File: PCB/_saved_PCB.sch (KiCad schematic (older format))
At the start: 9 parts, among them P1 Power, P2 Analog, P3 Digital, P4 Digital, P5 CONN_01X01, P6 CONN_01X01, P7 CONN_01X01, P8 CONN_01X01

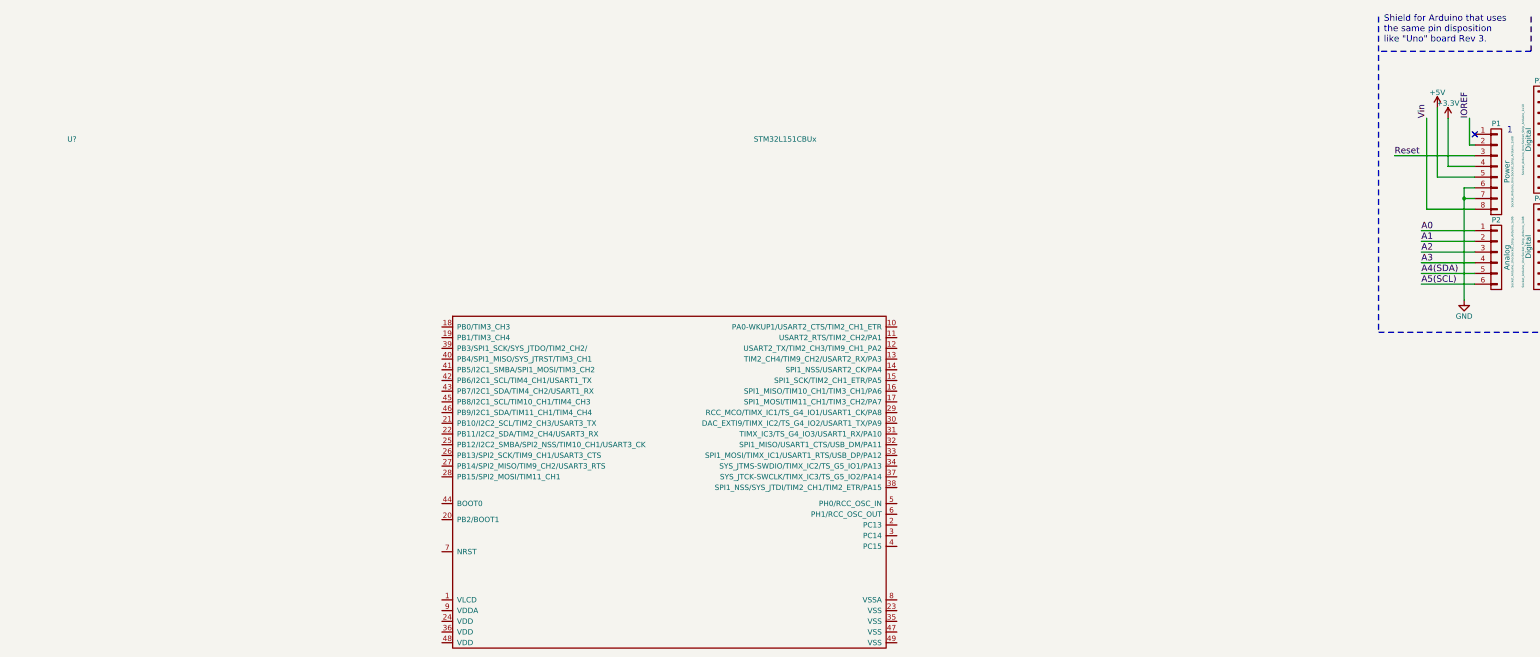
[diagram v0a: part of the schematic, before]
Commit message: add license
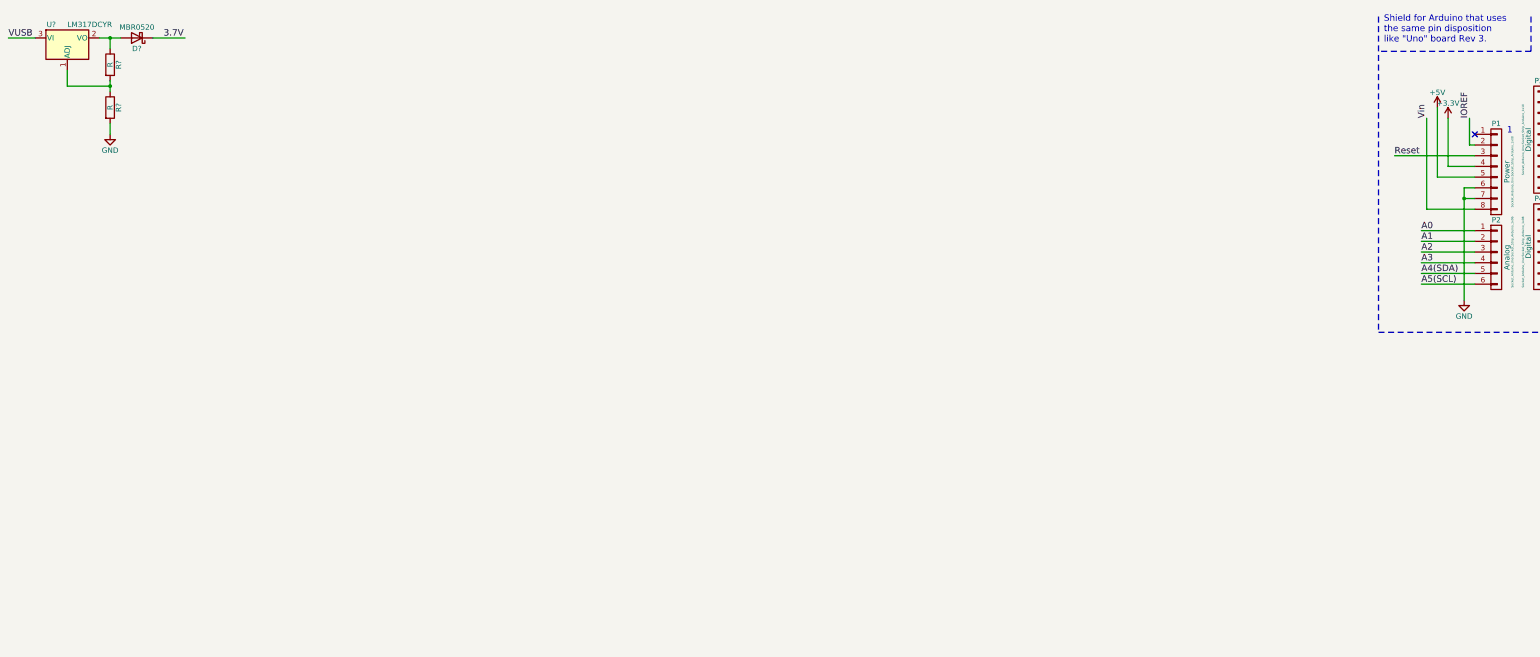
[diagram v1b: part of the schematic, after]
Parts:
- removed U?: STM32L151CBUx, UFQFPN48, symbol STM32L151CBUx
- added D?: MBR0520, Diode_SMD:D_SOD-123, symbol MBR0520
- added R? (x2): R, symbol R
- added U?: LM317DCYR, symbol LM317_3PinPackage
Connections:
- net GND: now also R?.2
- new net: R?.1, R?.2, U?.1 (ADJ)
- new net: D?.2 (A), R?.1, U?.2 (VO)
- new net 3.7V: D?.1 (K)
- new net VUSB: U?.3 (VI)
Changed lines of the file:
@@
 	15150 1500 15150 3150
 Wire Wire Line
-	14150 2100 14150 2200
-Wire Wire Line
-	14150 2200 14150 3150
+	14150 2100 14150 3150
 Wire Notes Line
 	13350 500  13350 3450
@@
 	15550 1000 15550 500
 $Comp
-L STM32L151CBUx U?
-U 1 1 5A66E205
-P 4600 3400
-F 0 "U?" H 1100 5125 50  0000 L BNN
-F 1 "STM32L151CBUx" H 8100 5125 50  0000 R BNN
-F 2 "UFQFPN48" H 8100 5075 50  0001 R TNN
-F 3 "" H 4600 3400 50  0001 C CNN
-	1    4600 3400
+L LM317_3PinPackage U?
+U 1 1 5A66EDE5
+P 1100 700
+F 0 "U?" H 950 825 50  0000 C CNN
+F 1 "LM317DCYR" H 1100 825 50  0000 L CNN
+F 2 "" H 1100 950 50  0001 C CIN
+F 3 "" H 1100 700 50  0001 C CNN
+	1    1100 700
 	1    0    0    -1
 $EndComp
+$Comp
+L MBR0520 D?
+U 1 1 5A66F152
+P 1750 700
+F 0 "D?" H 1750 800 50  0000 C CNN
+F 1 "MBR0520" H 1750 600 50  0000 C CNN
+F 2 "Diode_SMD:D_SOD-123" H 1750 525 50  0001 C CNN
+F 3 "" H 1750 700 50  0001 C CNN
+	1    1750 700
+	-1   0    0    1
+$EndComp
+Wire Wire Line
+	1400 700  1600 700
+$Comp
+L R R?
+U 1 1 5A66F3B1
+P 1500 950
+F 0 "R?" V 1580 950 50  0000 C CNN
+F 1 "R" V 1500 950 50  0000 C CNN
+F 2 "" V 1430 950 50  0001 C CNN
+F 3 "" H 1500 950 50  0001 C CNN
+	1    1500 950
+	1    0    0    -1
+$EndComp
+$Comp
+L R R?
+U 1 1 5A66F406
+P 1500 1350
+F 0 "R?" V 1580 1350 50  0000 C CNN
+F 1 "R" V 1500 1350 50  0000 C CNN
+F 2 "" V 1430 1350 50  0001 C CNN
+F 3 "" H 1500 1350 50  0001 C CNN
+	1    1500 1350
+	1    0    0    -1
+$EndComp
+Wire Wire Line
+	1500 800  1500 700
+Connection ~ 1500 700
+Wire Wire Line
+	1500 1100 1500 1200
+Wire Wire Line
+	1100 1000 1100 1150
+Wire Wire Line
+	1100 1150 1500 1150
+Connection ~ 1500 1150
+$Comp
+L GND #PWR?
+U 1 1 5A66F652
+P 1500 1600
+F 0 "#PWR?" H 1500 1350 50  0001 C CNN
+F 1 "GND" H 1500 1450 50  0000 C CNN
+F 2 "" H 1500 1600 50  0001 C CNN
+F 3 "" H 1500 1600 50  0001 C CNN
+	1    1500 1600
+	1    0    0    -1
+$EndComp
+Wire Wire Line
+	1500 1500 1500 1600
+Wire Wire Line
+	800  700  550  700
+Text Label 550  700  0    60   ~ 0
+VUSB
+Wire Wire Line
+	1900 700  2200 700
+Text Label 2000 700  0    60   ~ 0
+3.7V
 $EndSCHEMATC
